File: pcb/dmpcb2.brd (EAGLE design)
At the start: 100 x 100 mm, 70 parts, among them IC1 7805DT, IC2 L293D, IC4 LM358D, IC5 LM358D, J7 SJ-3523-SMT-TR, Q1 IRF530, Q2 IRF530

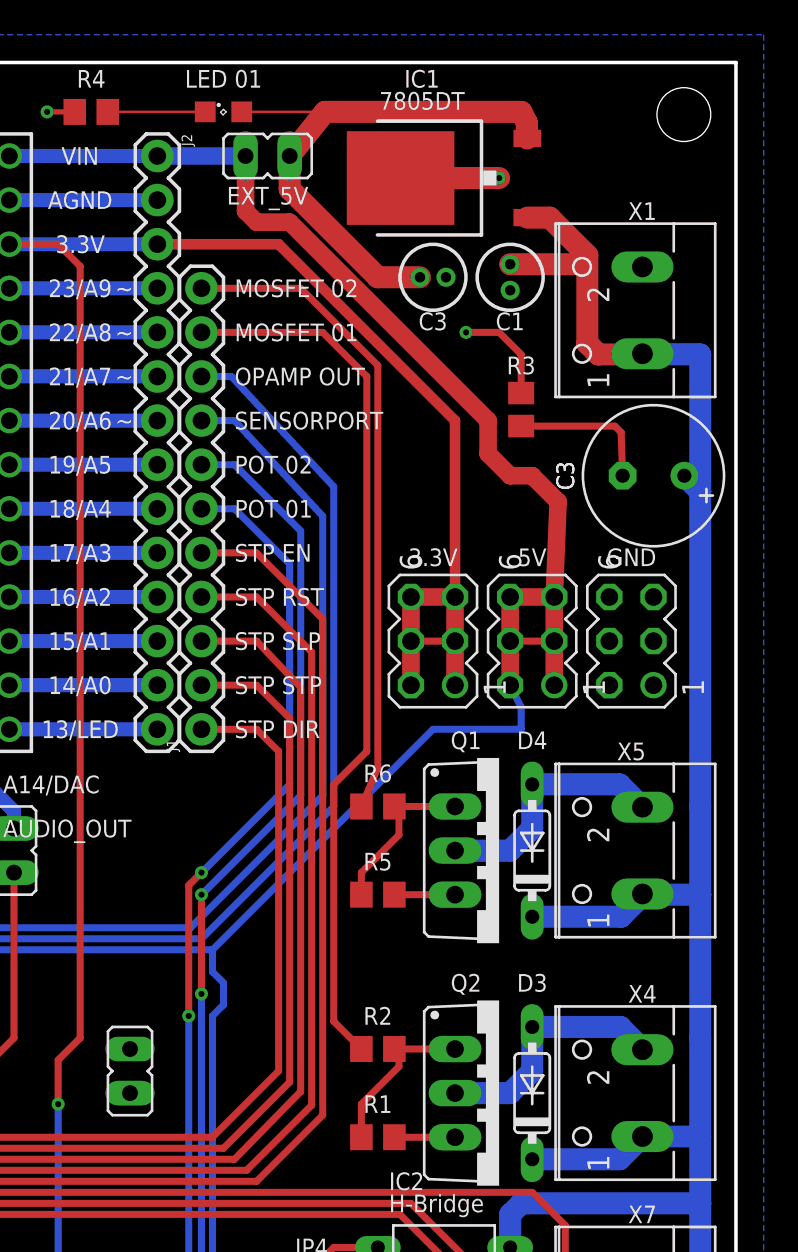
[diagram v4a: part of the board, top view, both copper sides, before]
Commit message: added possibilty to jump out the lm7805
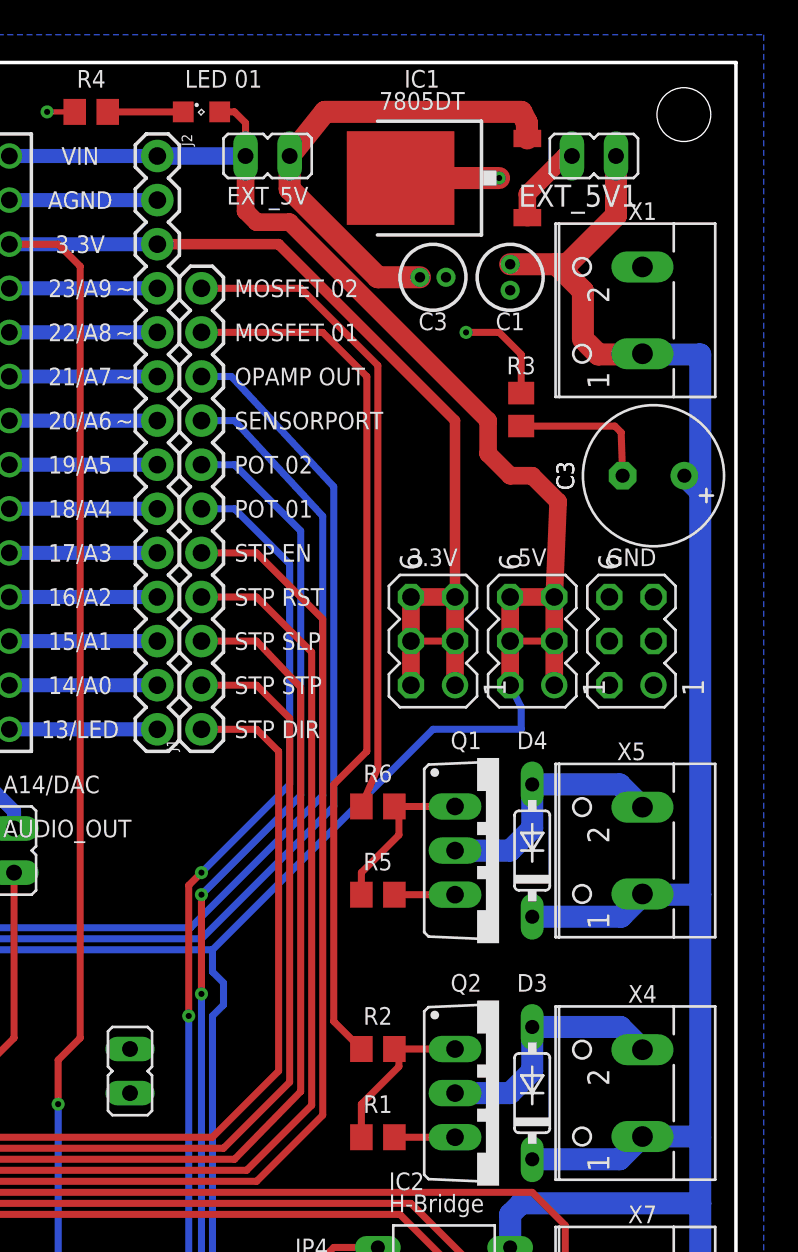
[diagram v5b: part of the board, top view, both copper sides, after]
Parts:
- added EXT_5V1: (no value), jumper:JP1
- moved LED_01 1.27 mm to (69.2, 97.2)
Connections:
- new net N$19: EXT_5V1.2, IC1.1
- net +5V: now also LED_01.A
- net N$25: no longer LED_01.A
- net V+: now also EXT_5V1.1; no longer IC1.1
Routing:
- net N$19: track 0.00 -> 4.84 mm
- net N$25: track 32.5 -> 27.7 mm
- net +5V: track 358.0 -> 361.6 mm
- net V+: track 222.2 -> 224.1 mm
- net N$9: track 5.62 -> 4.35 mm
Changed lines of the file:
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@@
 <attribute name="VALUE" x="15.748" y="60.579" size="1.27" layer="27" ratio="10" rot="R270"/>
 </element>
-<element name="LED_01" library="led" library_urn="urn:adsk.eagle:library:259" package="SML0805" package3d_urn="urn:adsk.eagle:package:15830/1" value="" x="70.485" y="97.155" smashed="yes">
-<attribute name="POPULARITY" value="17" x="70.485" y="97.155" size="1.778" layer="27" display="off"/>
-<attribute name="VALUE" x="68.985" y="95.155" size="1.27" layer="27"/>
+<element name="LED_01" library="led" library_urn="urn:adsk.eagle:library:259" package="SML0805" package3d_urn="urn:adsk.eagle:package:15830/1" value="" x="69.215" y="97.155" smashed="yes">
+<attribute name="POPULARITY" value="17" x="69.215" y="97.155" size="1.778" layer="27" display="off"/>
+<attribute name="VALUE" x="67.715" y="95.155" size="1.27" layer="27"/>
 </element>
 <element name="Q1" library="transistor-power" library_urn="urn:adsk.eagle:library:400" package="TO220BV" package3d_urn="urn:adsk.eagle:package:29484/3" value="IRF530" x="86.36" y="54.61" smashed="yes" rot="R270">
@@
 <element name="J4" library="SparkFun-Connectors" library_urn="urn:adsk.eagle:library:513" package="1X03_LOCK_LONGPADS" package3d_urn="urn:adsk.eagle:package:38065/1" value="" x="75.565" y="27.94" smashed="yes" rot="R270">
 <attribute name="VALUE" x="73.152" y="29.21" size="0.6096" layer="27" font="vector" ratio="20" rot="R270"/>
+</element>
+<element name="EXT_5V1" library="jumper" library_urn="urn:adsk.eagle:library:252" package="JP1" package3d_urn="urn:adsk.eagle:package:15455/1" value="" x="91.821" y="94.615" smashed="yes" rot="R90">
+<attribute name="NAME" x="94.361" y="92.964" size="1.27" layer="25" ratio="10" rot="R180"/>
+<attribute name="POPULARITY" value="61" x="91.821" y="94.615" size="1.778" layer="27" rot="R90" display="off"/>
+<attribute name="VALUE" x="94.361" y="97.536" size="1.27" layer="27" ratio="10" rot="R180"/>
 </element>
 </elements>
@@
 </signal>
 <signal name="V+">
-<contactref element="IC1" pad="1"/>
 <contactref element="C1" pad="+"/>
 <contactref element="C3" pad="+"/>
@@
 <contactref element="D4" pad="C"/>
 <contactref element="JP1" pad="1"/>
-<wire x1="97.9424" y1="43.815" x2="97.9424" y2="52.07" width="1.27" layer="16"/>
-<wire x1="97.9424" y1="52.07" x2="97.9424" y2="57.15" width="1.27" layer="16"/>
+<wire x1="97.9424" y1="38.1" x2="97.9424" y2="52.07" width="1.27" layer="16"/>
 <wire x1="27.94" y1="1.7526" x2="90.805" y2="1.7526" width="1.27" layer="16"/>
 <wire x1="90.805" y1="1.7526" x2="97.9424" y2="8.89" width="1.27" layer="16"/>
@@
 <contactref element="X5" pad="1"/>
 <wire x1="97.9424" y1="34.29" x2="97.9424" y2="38.1" width="1.27" layer="16"/>
-<wire x1="97.9424" y1="38.1" x2="97.9424" y2="43.815" width="1.27" layer="16"/>
 <wire x1="86.995" y1="31.75" x2="86.995" y2="33.655" width="1.27" layer="16"/>
 <wire x1="86.995" y1="33.655" x2="87.63" y2="34.29" width="1.27" layer="16"/>
 <wire x1="87.63" y1="34.29" x2="97.9424" y2="34.29" width="1.27" layer="16"/>
 <wire x1="97.028" y1="76.2" x2="97.9424" y2="75.2856" width="1.27" layer="16"/>
-<wire x1="97.9424" y1="75.2856" x2="97.9424" y2="57.15" width="1.27" layer="16"/>
+<wire x1="97.9424" y1="75.2856" x2="97.9424" y2="52.07" width="1.27" layer="16"/>
 <wire x1="97.9424" y1="83.185" x2="97.9424" y2="75.2856" width="1.27" layer="16"/>
 <wire x1="20.32" y1="15.875" x2="23.495" y2="15.875" width="1.27" layer="16"/>
@@
 <wire x1="23.495" y1="15.875" x2="26.67" y2="12.7" width="1.27" layer="16"/>
 <wire x1="26.67" y1="12.7" x2="26.67" y2="3.0226" width="1.27" layer="16"/>
-<wire x1="89.275" y1="91.065" x2="91.44" y2="88.9" width="1.27" layer="1"/>
-<wire x1="91.44" y1="88.9" x2="91.44" y2="83.82" width="1.27" layer="1"/>
 <wire x1="91.44" y1="83.82" x2="92.075" y2="83.185" width="1.27" layer="1"/>
 <wire x1="92.075" y1="83.185" x2="94.575" y2="83.185" width="1.27" layer="1"/>
 <wire x1="94.575" y1="83.185" x2="94.615" y2="83.225" width="0.1524" layer="1"/>
-<wire x1="89.275" y1="91.065" x2="87.985" y2="91.065" width="1.27" layer="1"/>
-<wire x1="91.44" y1="88.9" x2="90.92" y2="88.38" width="0.1524" layer="1"/>
-<wire x1="90.92" y1="88.38" x2="86.995" y2="88.38" width="1.27" layer="1"/>
+<wire x1="86.995" y1="88.38" x2="89.65" y2="88.38" width="1.27" layer="1"/>
 <wire x1="97.9424" y1="83.185" x2="94.655" y2="83.185" width="1.27" layer="16"/>
 <wire x1="94.655" y1="83.185" x2="94.615" y2="83.225" width="0.1524" layer="16"/>
@@
 <wire x1="94.615" y1="38.14" x2="97.9024" y2="38.14" width="1.27" layer="16"/>
 <wire x1="97.9024" y1="38.14" x2="97.9424" y2="38.1" width="0.1524" layer="16"/>
+<contactref element="EXT_5V1" pad="1"/>
+<wire x1="89.65" y1="88.38" x2="91.186" y2="86.844" width="1.27" layer="1"/>
+<wire x1="91.186" y1="84.074" x2="91.44" y2="83.82" width="1.016" layer="1"/>
+<wire x1="91.186" y1="86.844" x2="91.186" y2="84.074" width="1.27" layer="1"/>
+<wire x1="93.091" y1="94.615" x2="93.091" y2="91.186" width="1.27" layer="1"/>
+<wire x1="90.285" y1="88.38" x2="89.65" y2="88.38" width="1.27" layer="1"/>
+<wire x1="93.091" y1="91.186" x2="90.285" y2="88.38" width="1.27" layer="1"/>
 </signal>
 <signal name="+5V">
@@
 <wire x1="74.295" y1="90.805" x2="72.39" y2="90.805" width="1.016" layer="1"/>
 <wire x1="71.755" y1="91.44" x2="71.755" y2="94.615" width="1.016" layer="1"/>
+<contactref element="LED_01" pad="A"/>
+<wire x1="71.755" y1="94.615" x2="71.755" y2="96.52" width="0.4064" layer="1"/>
+<wire x1="71.755" y1="96.52" x2="71.12" y2="97.155" width="0.4064" layer="1"/>
+<wire x1="71.12" y1="97.155" x2="70.265" y2="97.155" width="0.4064" layer="1"/>
 </signal>
 <signal name="MM92">
@@
 <contactref element="LED_01" pad="C"/>
 <contactref element="R4" pad="2"/>
-<wire x1="69.435" y1="97.155" x2="63.815" y2="97.155" width="0.1524" layer="1"/>
+<wire x1="68.165" y1="97.155" x2="63.815" y2="97.155" width="0.4064" layer="1"/>
 </signal>
 <signal name="MOSFET01">
@@
 <contactref element="IC1" pad="2"/>
 <contactref element="C2" pad="+"/>
-<contactref element="LED_01" pad="A"/>
 <contactref element="EXT_5V" pad="1"/>
 <wire x1="74.295" y1="94.615" x2="76.327" y2="97.155" width="1.27" layer="1"/>
@@
 <wire x1="79.375" y1="87.63" x2="74.295" y2="92.71" width="1.27" layer="1"/>
 <wire x1="74.295" y1="92.71" x2="74.295" y2="94.615" width="1.27" layer="1"/>
-<wire x1="71.535" y1="97.155" x2="76.327" y2="97.155" width="0.1524" layer="1"/>
 </signal>
 <signal name="M1">
@@
 <wire x1="78.105" y1="16.51" x2="79.375" y2="16.51" width="0.4064" layer="1"/>
 </signal>
+<signal name="N$19">
+<contactref element="EXT_5V1" pad="2"/>
+<contactref element="IC1" pad="1"/>
+<wire x1="87.985" y1="91.065" x2="87.985" y2="92.43" width="1.016" layer="1"/>
+<wire x1="90.17" y1="94.615" x2="90.551" y2="94.615" width="1.016" layer="1"/>
+<wire x1="87.985" y1="92.43" x2="90.17" y2="94.615" width="1.016" layer="1"/>
+</signal>
 </signals>
